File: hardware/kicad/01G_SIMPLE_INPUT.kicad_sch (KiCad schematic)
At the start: 3 parts, among them J901 BAT_ACC_GND_PIGTAIL

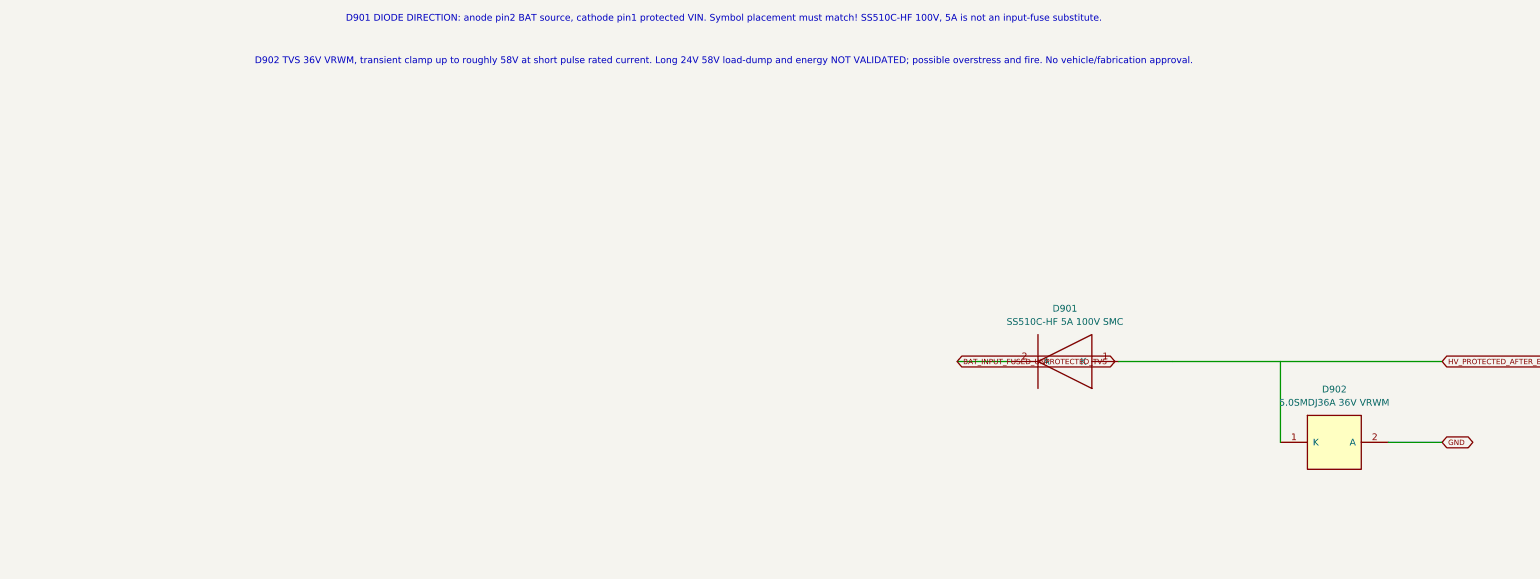
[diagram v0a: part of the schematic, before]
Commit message: Replace under-clamped input with 58V flat-clamp candidate and 1kV reverse rectifier
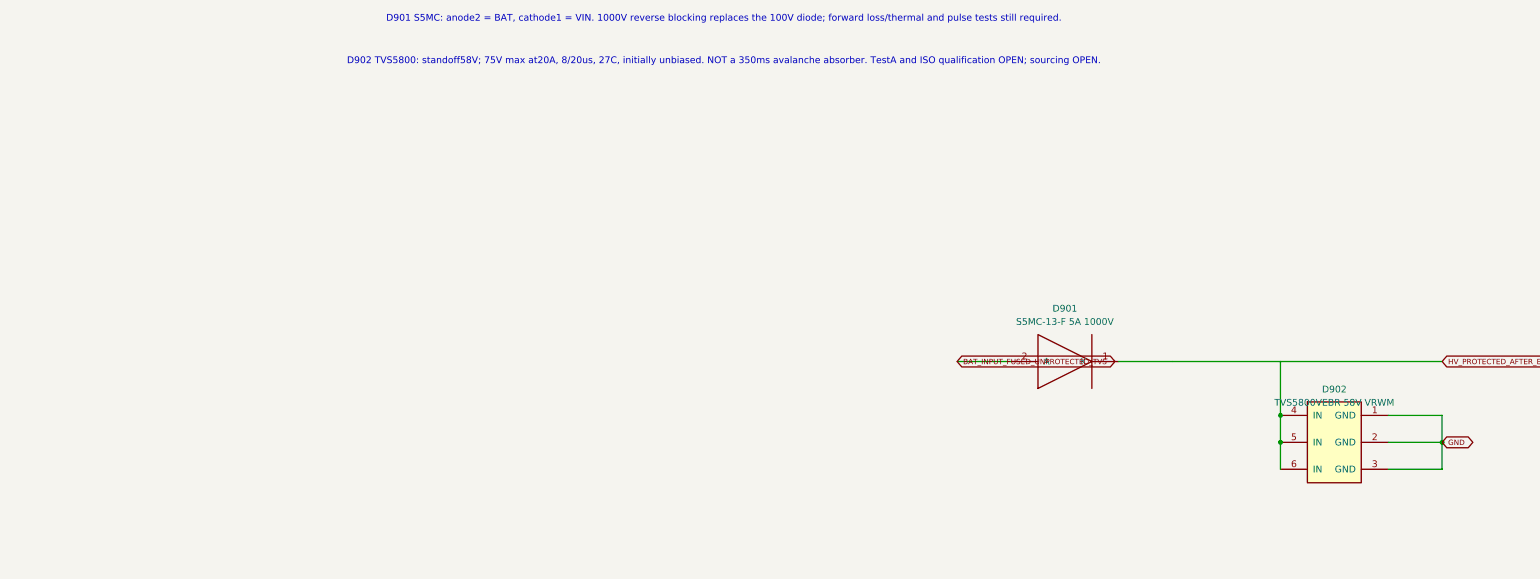
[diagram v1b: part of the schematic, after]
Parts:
- D901: value SS510C-HF 5A 100V SMC -> S5MC-13-F 5A 1000V; footprint Diode_SMD:D_SMC -> Tripmaster:D_S5MC_SMC; symbol TripTracer_V1:SS510C_HF_SMC -> TripTracer_V1:S5MC_SMC
- D902: value 5.0SMDJ36A 36V VRWM -> TVS5800VEBR 58V VRWM; footprint Diode_SMD:D_SMC -> Tripmaster:D_TVS5800_VEB0006A; symbol TripTracer_V1:5_0SMDJ36A -> TripTracer_V1:TVS5800_VEB
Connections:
- net GND: now also D902.1 (GND), D902.3 (GND)
- net HV_PROTECTED_AFTER_EFUSE: now also D902.4 (IN), D902.5 (IN), D902.6 (IN); no longer D902.1 (K)
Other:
- note added: "D901 S5MC: anode2 = BAT, cathode1 = VIN. 1000V reverse blocking replaces the 100V diode; forward loss/thermal and pulse tests still required."
- note added: "D902 TVS5800: standoff58V; 75V max at20A, 8/20us, 27C, initially unbiased. NOT a 350ms avalanche absorber. TestA and ISO qualification OPEN; sourcing OPEN."
- note removed: "D901 DIODE DIRECTION: anode pin2 BAT source, cathode pin1 protected VIN. Symbol placement must match! SS510C-HF 100V, 5A is not an input-fuse substitute."
- note removed: "D902 TVS 36V VRWM, transient clamp up to roughly 58V at short pulse rated current. Long 24V 58V load-dump and energy NOT VALIDATED; possible overstress and fire. No vehicle/fabrication approval."

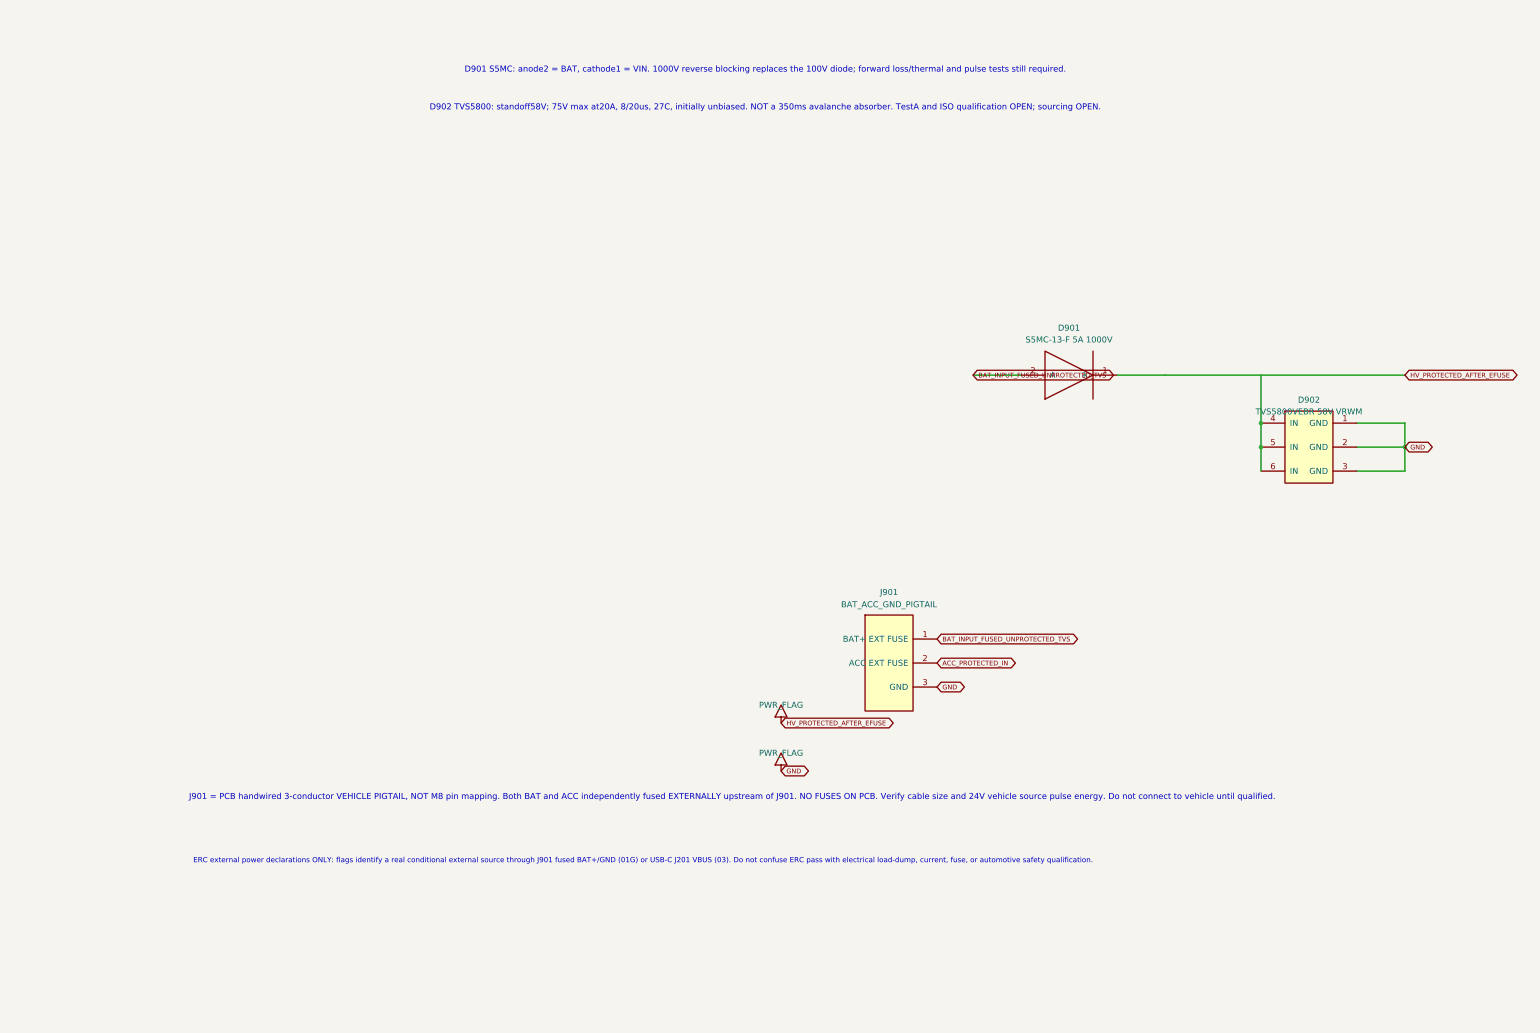
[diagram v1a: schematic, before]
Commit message: Make input protection and ACC interfaces readable in native schematic PDF
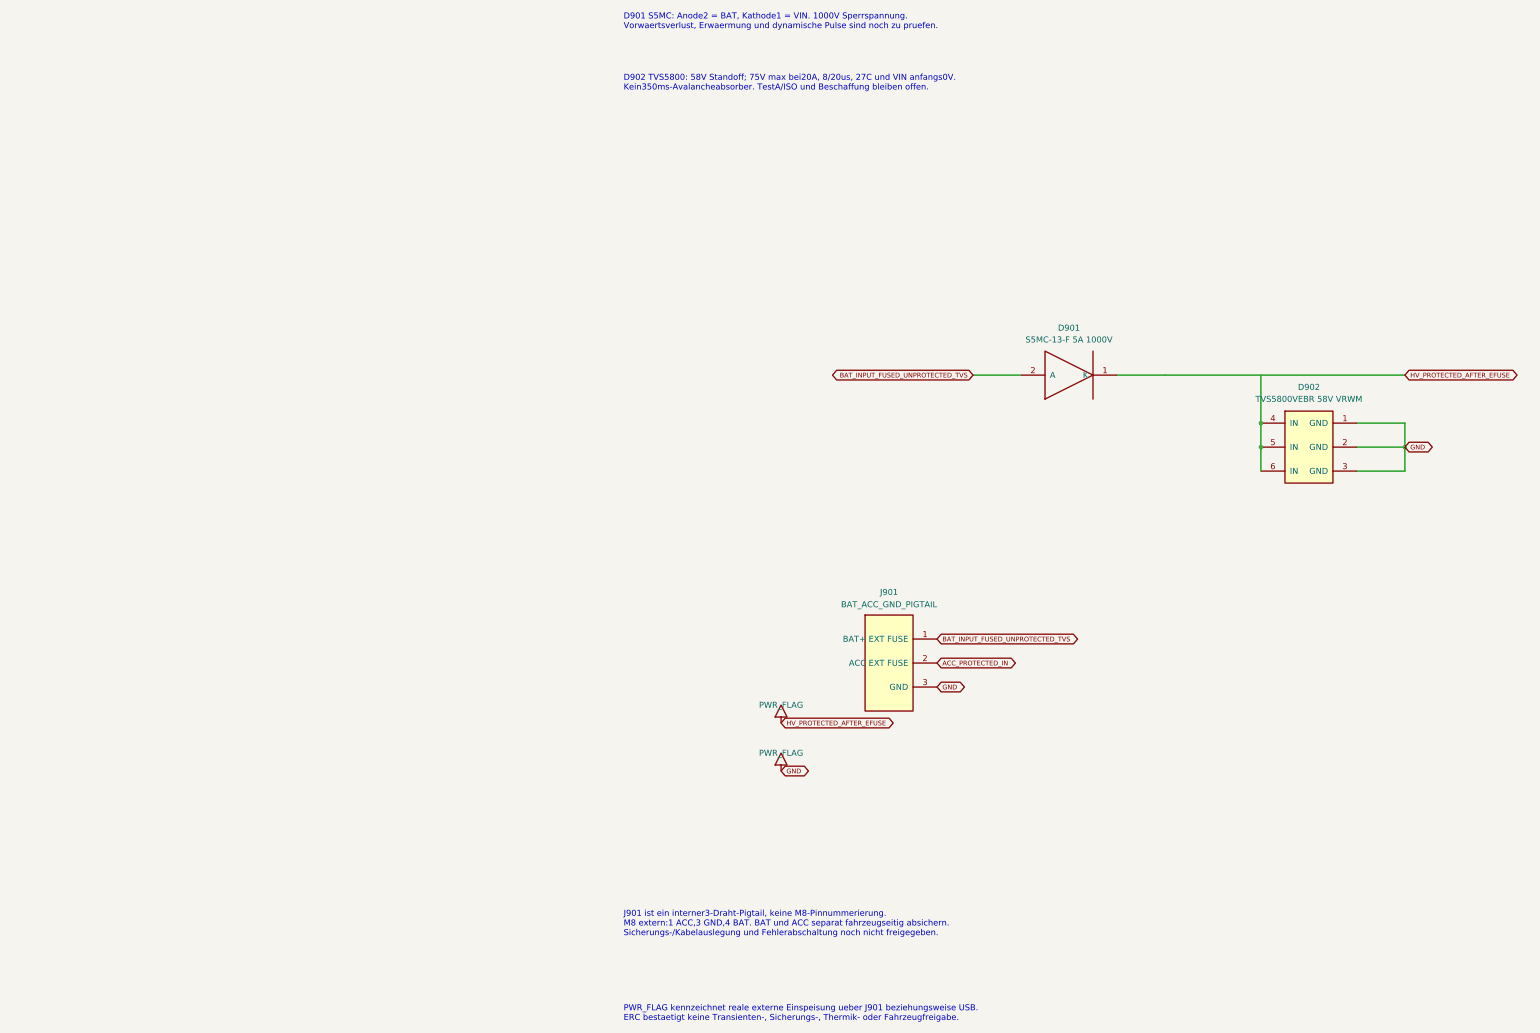
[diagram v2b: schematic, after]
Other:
- note added: "D901 S5MC: Anode2 = BAT, Kathode1 = VIN. 1000V Sperrspannung. Vorwaertsverlust, Erwaermung und dynamische Pulse sind noch zu pruefen."
- note added: "D902 TVS5800: 58V Standoff; 75V max bei20A, 8/20us, 27C und VIN anfangs0V. Kein350ms-Avalancheabsorber. TestA/ISO und Beschaffung bleiben offen."
- note added: "J901 ist ein interner3-Draht-Pigtail, keine M8-Pinnummerierung. M8 extern:1 ACC,3 GND,4 BAT. BAT und ACC separat fahrzeugseitig absichern. Sicherungs-/Kabelauslegung und Fehlerabschaltung noch nicht freigegeben."
- note added: "PWR_FLAG kennzeichnet reale externe Einspeisung ueber J901 beziehungsweise USB. ERC bestaetigt keine Transienten-, Sicherungs-, Thermik- oder Fahrzeugfreigabe."
- note removed: "D901 S5MC: anode2 = BAT, cathode1 = VIN. 1000V reverse blocking replaces the 100V diode; forward loss/thermal and pulse tests still required."
- note removed: "D902 TVS5800: standoff58V; 75V max at20A, 8/20us, 27C, initially unbiased. NOT a 350ms avalanche absorber. TestA and ISO qualification OPEN; sourcing OPEN."
- note removed: "ERC external power declarations ONLY: flags identify a real conditional external source through J901 fused BAT+/GND (01G) or USB-C J201 VBUS (03). Do not confuse ERC pass with electrical load-dump, current, fuse, or automotive safety qualification."
- note removed: "J901 = PCB handwired 3-conductor VEHICLE PIGTAIL, NOT M8 pin mapping. Both BAT and ACC independently fused EXTERNALLY upstream of J901. NO FUSES ON PCB. Verify cable size and 24V vehicle source pulse energy. Do not connect to vehicle until qualified."

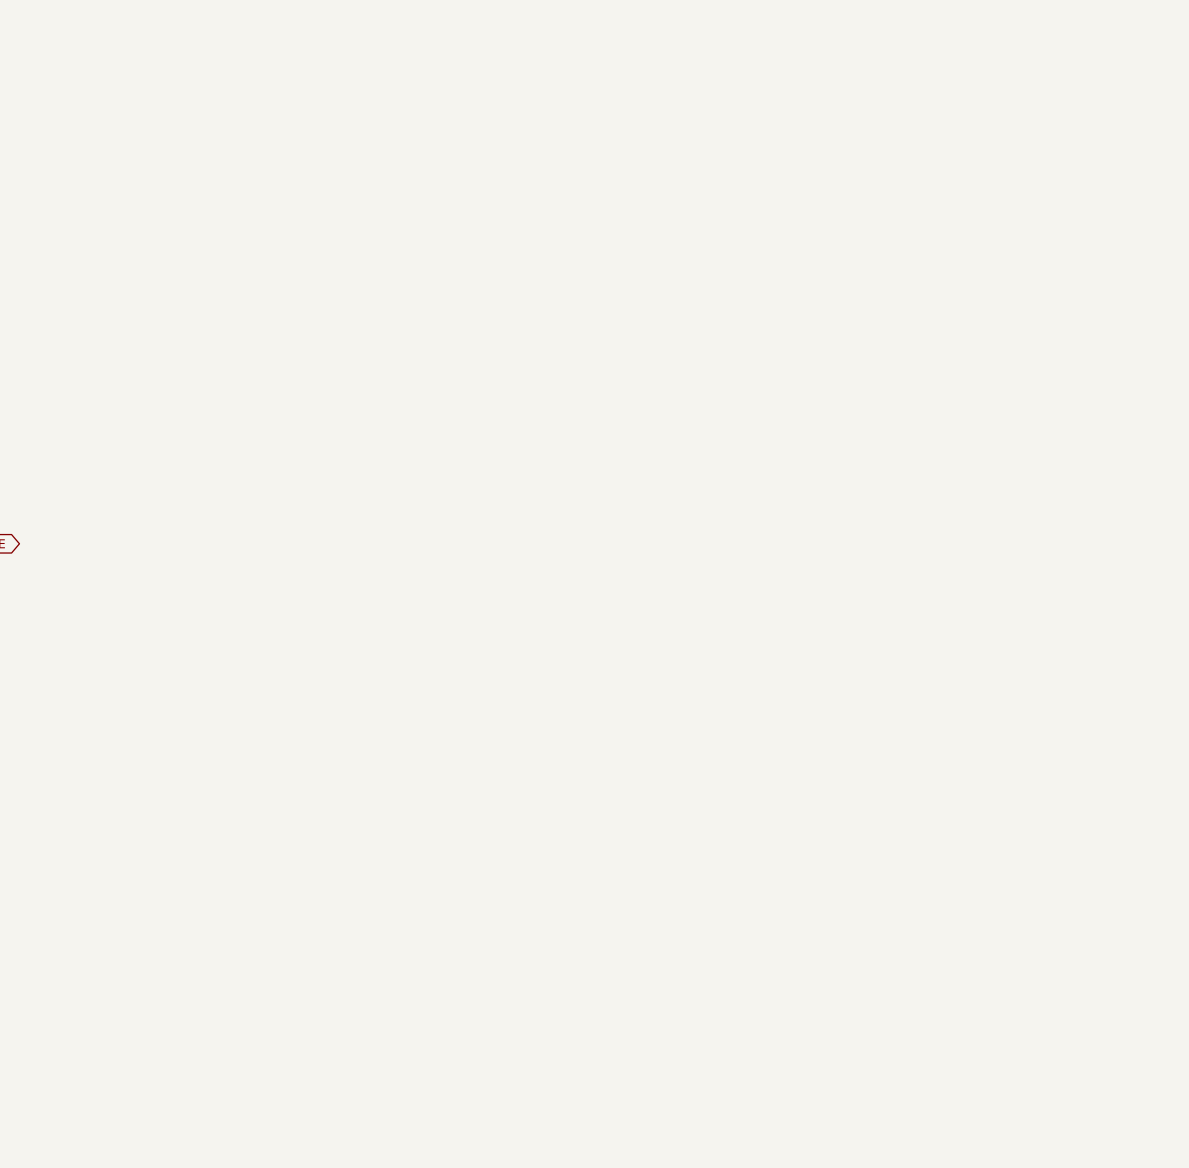
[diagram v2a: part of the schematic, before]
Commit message: Correct 9V HOLD for wiring loss and define replaceable source fuse candidates
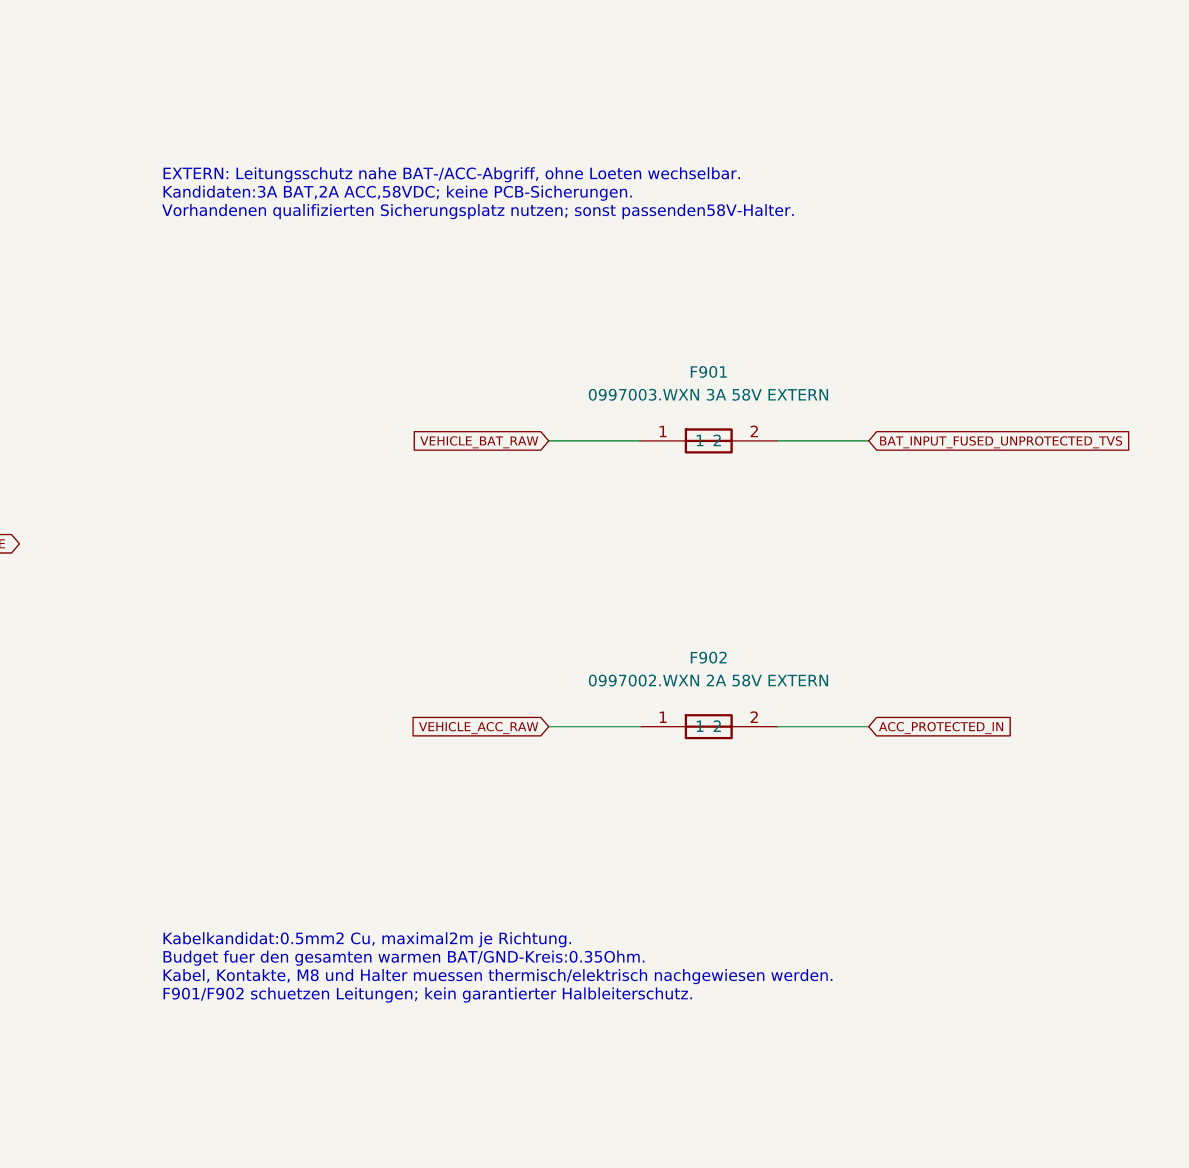
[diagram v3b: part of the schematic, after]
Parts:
- added F901: 0997003.WXN 3A 58V EXTERN, symbol TripTracer_V1:OFFBOARD_FUSE
- added F902: 0997002.WXN 2A 58V EXTERN, symbol TripTracer_V1:OFFBOARD_FUSE
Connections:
- net ACC_PROTECTED_IN: now also F902.2
- net BAT_INPUT_FUSED_UNPROTECTED_TVS: now also F901.2
- new net VEHICLE_ACC_RAW: F902.1
- new net VEHICLE_BAT_RAW: F901.1
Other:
- note added: "EXTERN: Leitungsschutz nahe BAT-/ACC-Abgriff, ohne Loeten wechselbar. Kandidaten:3A BAT,2A ACC,58VDC; keine PCB-Sicherungen. Vorhandenen qualifizierten Sicherungsplatz nutzen; sonst passenden58V-Halter."
- note added: "Kabelkandidat:0.5mm2 Cu, maximal2m je Richtung. Budget fuer den gesamten warmen BAT/GND-Kreis:0.35Ohm. Kabel, Kontakte, M8 und Halter muessen thermisch/elektrisch nachgewiesen werden. F901/F902 schuetzen Leitungen; kein garantierter Halbleiterschutz."
